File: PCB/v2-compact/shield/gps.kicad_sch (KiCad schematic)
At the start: 0 parts

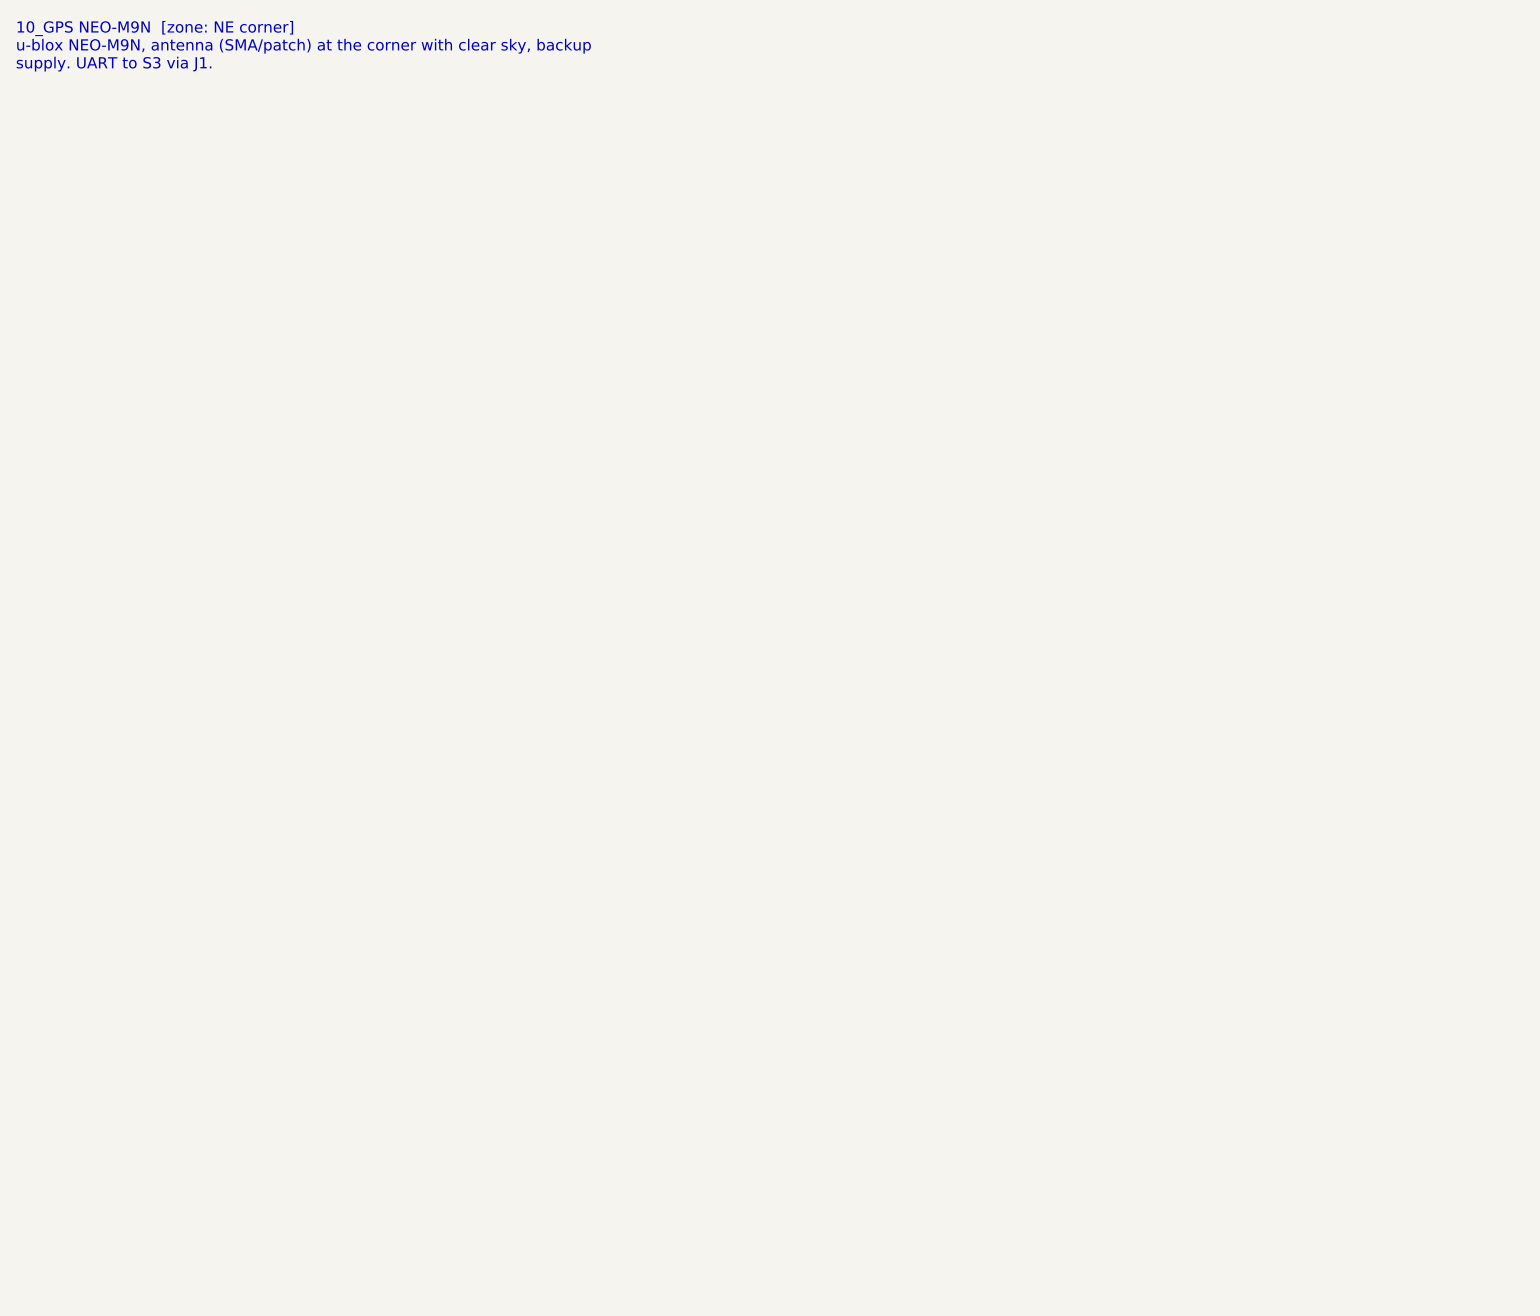
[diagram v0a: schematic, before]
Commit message: Schematics: capture PN532, GPS, IR, and both power sheets
- 07_NFC_PN532: I2C mode (I0/I1 set), 27.12MHz crystal, VMID cap, internal
  DVDD/SVDD regulator outputs correctly decoupled (not tied to 3V3), pull-ups;
  antenna pins flagged for the RF matching pass.
- 10_GPS: NEO-M9N UART to the C5, power + decoupling; bias-tee/antenna flagged.
- 11_IR: TSOP receiver + IR-LED transmitter (NPN driver).
- 02_Power (shield): local AP7361C LDO for the C5 rail + bulk caps + PWR_FLAGs.
- 01_Power_USB (main): USB-C, CC resistors, USBLC6 ESD, AP7361C 3V3 LDO.

All netlist-verified. Remaining ERC items are expected WIP (no-connects on unused
IC pins + power flags), to be cleaned once the MCU sheets tie in the shared nets.
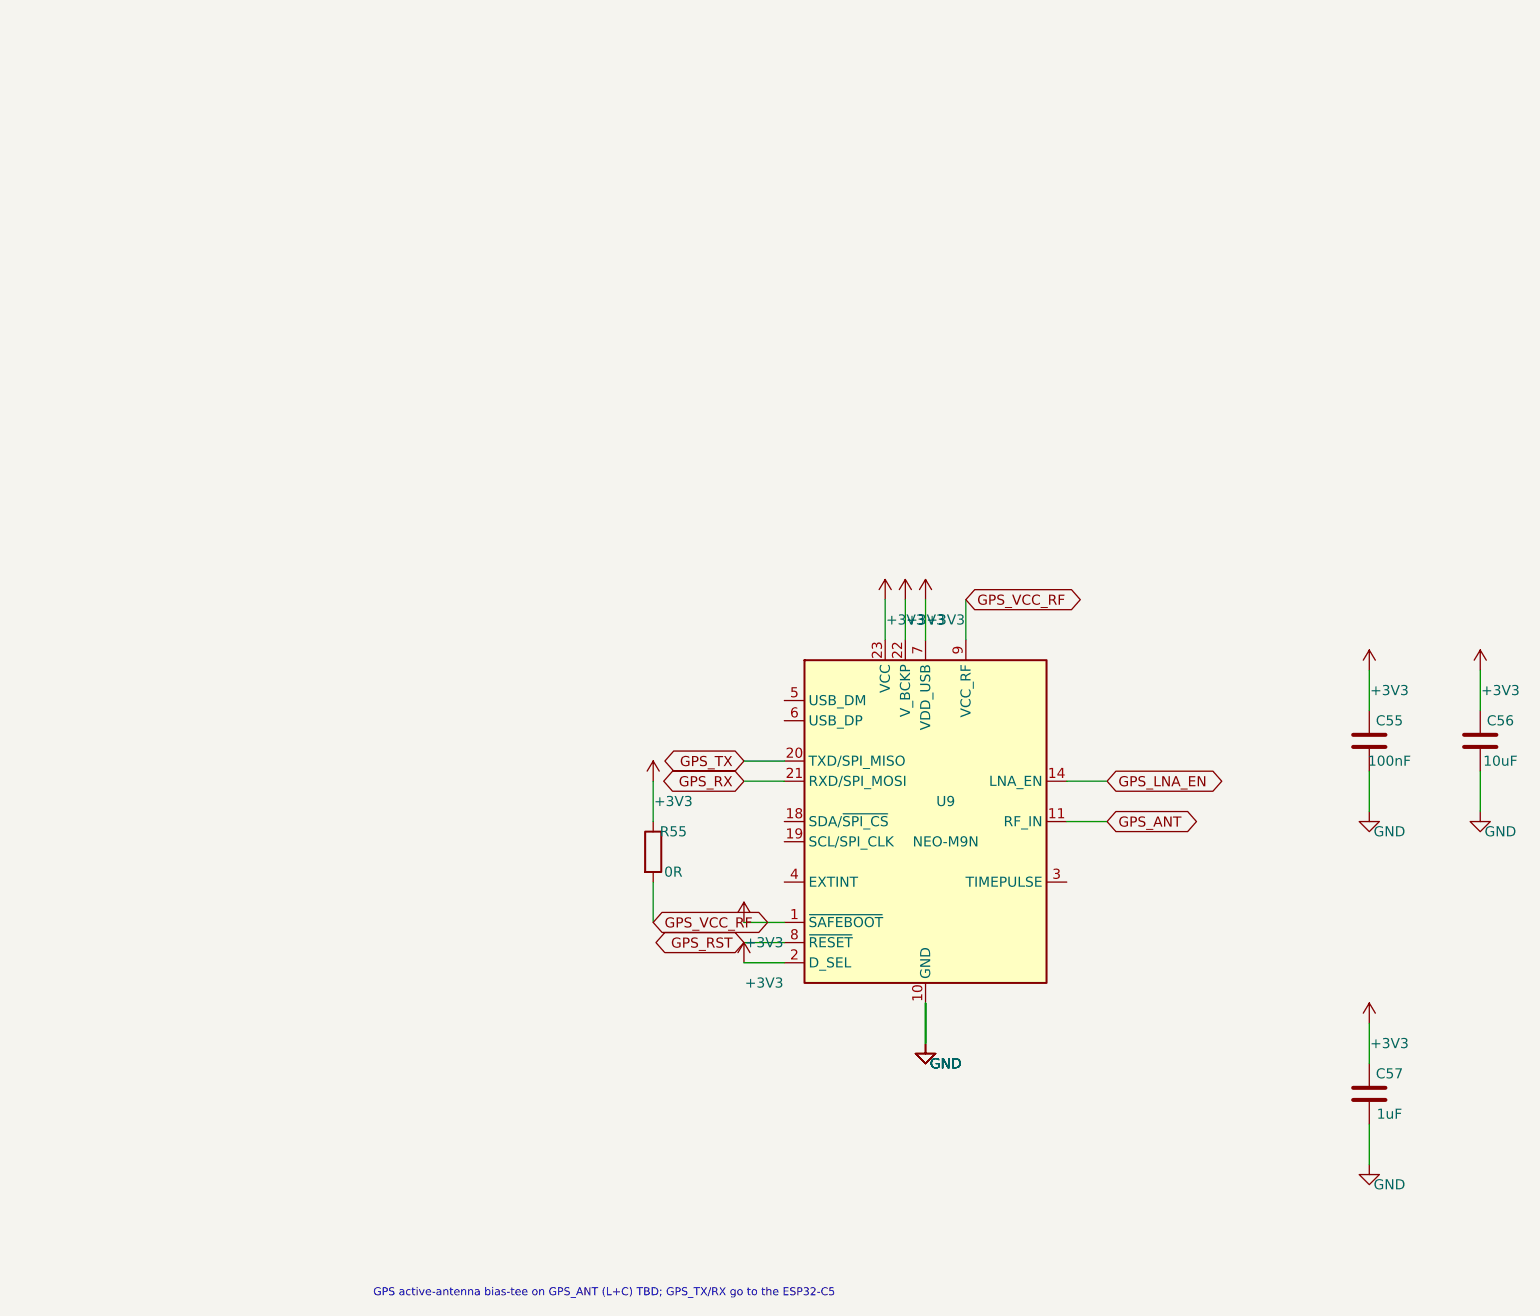
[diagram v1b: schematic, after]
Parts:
- added C55: 100nF, Capacitor_SMD:C_0402_1005Metric, symbol Device:C
- added C56: 10uF, Capacitor_SMD:C_0402_1005Metric, symbol Device:C
- added C57: 1uF, Capacitor_SMD:C_0402_1005Metric, symbol Device:C
- added R55: 0R, Resistor_SMD:R_0402_1005Metric, symbol Device:R
- added U9: NEO-M9N, symbol RF_GPS:NEO-M9N
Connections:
- new net +3V3: C55.1, C56.1, C57.1, R55.1, U9.1 (~{SAFEBOOT}), U9.2 (D_SEL), U9.22 (V_BCKP), U9.23 (VCC), U9.7 (VDD_USB)
- new net GND: C55.2, C56.2, C57.2, U9.10 (GND), U9.12 (GND), U9.13 (GND), U9.24 (GND)
- new net GPS_ANT: U9.11 (RF_IN)
- new net GPS_LNA_EN: U9.14 (LNA_EN)
- new net GPS_RST: U9.8 (~{RESET})
- new net GPS_RX: U9.21 (RXD/SPI_MOSI)
- new net GPS_TX: U9.20 (TXD/SPI_MISO)
- new net GPS_VCC_RF: R55.2, U9.9 (VCC_RF)
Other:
- note added: "GPS active-antenna bias-tee on GPS_ANT (L+C) TBD; GPS_TX/RX go to the ESP32-C5"
- note removed: "10_GPS NEO-M9N [zone: NE corner] u-blox NEO-M9N, antenna (SMA/patch) at the corner with clear sky, backup supply. UART to S3 via J1."

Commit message: Schematics: ESP32-C5 hub sheet with MCP23S17 CS/IO expander
The C5's ~22 GPIO cannot drive all the radio control lines directly, so per the
plan the C5 sheet adds an MCP23S17 SPI I/O expander on the shield:
- C5 masters the SPI spine (SCK/MOSI/MISO), talks to the S3 over UART0 (also on
  the J40 prog header), and drives the timing-critical lines directly (the three
  nRF24 CE lines, SX1262 BUSY).
- MCP23S17 (U42) generates the seven chip-selects + SX1262 reset on its GPA
  outputs and reads the radio IRQs on its GPB inputs, all local to the shield.
- EN/boot RC + pull-ups, decoupling, U.FL on C5_ANT.

Netlist-verified: SPI_SCK/MISO reach every slave + master + expander; FLASH_CS
and the NRFn_CSN come from the expander outputs; C5_TX reaches J1 and the header.
Also renamed duplicate C55/C56 refs on the GPS sheet.
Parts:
- removed C55: 100nF, Capacitor_SMD:C_0402_1005Metric, symbol Device:C
- removed C56: 10uF, Capacitor_SMD:C_0402_1005Metric, symbol Device:C
- removed C57: 1uF, Capacitor_SMD:C_0402_1005Metric, symbol Device:C
- added C70: 100nF, Capacitor_SMD:C_0402_1005Metric, symbol Device:C
- added C71: 10uF, Capacitor_SMD:C_0402_1005Metric, symbol Device:C
- added C72: 1uF, Capacitor_SMD:C_0402_1005Metric, symbol Device:C
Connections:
- net +3V3: now also C70.1, C71.1, C72.1
- net GND: now also C70.2, C71.2, C72.2

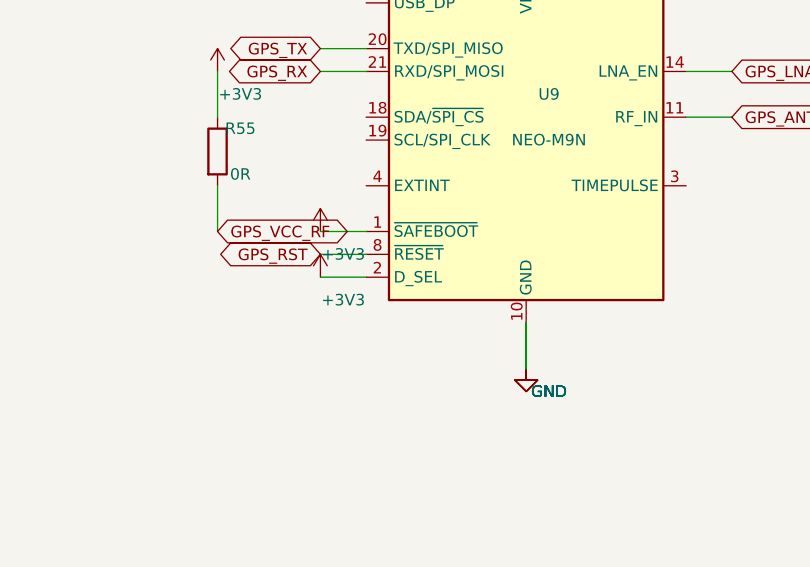
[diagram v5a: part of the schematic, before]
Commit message: Schematics: cleanup - HTRC110 footprint (SOIC-14), reset pull-ups (CC1200/GPS), RV1106 power flags
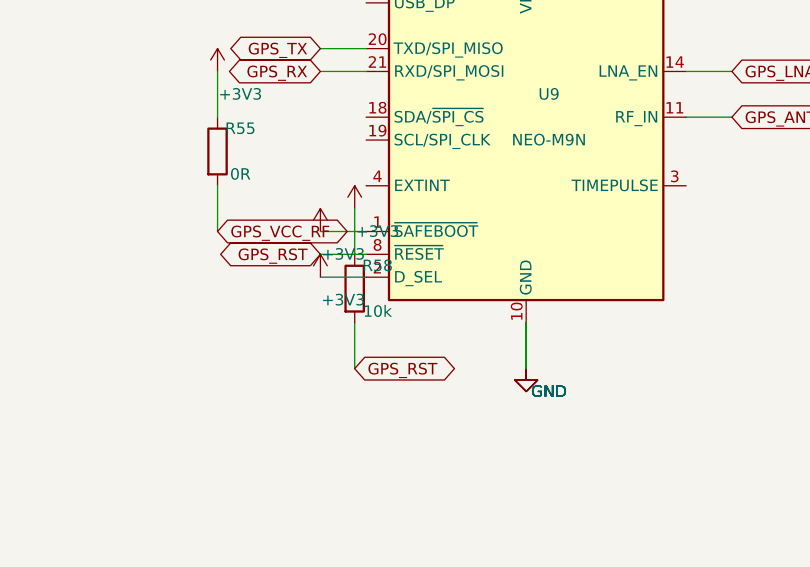
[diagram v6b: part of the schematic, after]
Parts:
- added R58: 10k, Resistor_SMD:R_0402_1005Metric, symbol Device:R
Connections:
- net +3V3: now also R58.1
- net GPS_RST: now also R58.2

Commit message: PCB: import schematic netlists onto both boards (parts placed + nets assigned)
Load every footprint from the schematic into the floorplan-skeleton boards,
place each in its subsystem's zone (grid-spread, back-side sheets flipped), and
assign all nets. Shield: 79 parts, 419 pad-nets, 153 nets. Main: 29 parts,
150 pad-nets, 57 nets. Register the Espressif footprint library; add a
placeholder Core1106 SoM footprint; assign the C5 (Espressif), NEO-M9N (ublox_NEO)
and CC1101 (2x4 header) module footprints.

This is the initial import: every part is on its board with the full ratsnest,
ready for placement refinement and routing.
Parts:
- U9: footprint (none) -> RF_GPS:ublox_NEO
